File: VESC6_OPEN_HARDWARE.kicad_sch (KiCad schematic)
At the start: 21 parts, among them P1 USB_OTG, P2 TS_CAN, P3 SWD, P4 HALL/Encoder, P7 Custom

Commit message: started power stage
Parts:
- removed TP1, TP2: TestPoint, TestPoint:TestPoint_Pad_D1.5mm, symbol Connector:TestPoint
- P7: symbol Intra-Drive-Motor-Controller-V1-rescue:Connector_10-Pin-SJG_KiCad_Library -> Connector:Conn_01x08_Pin

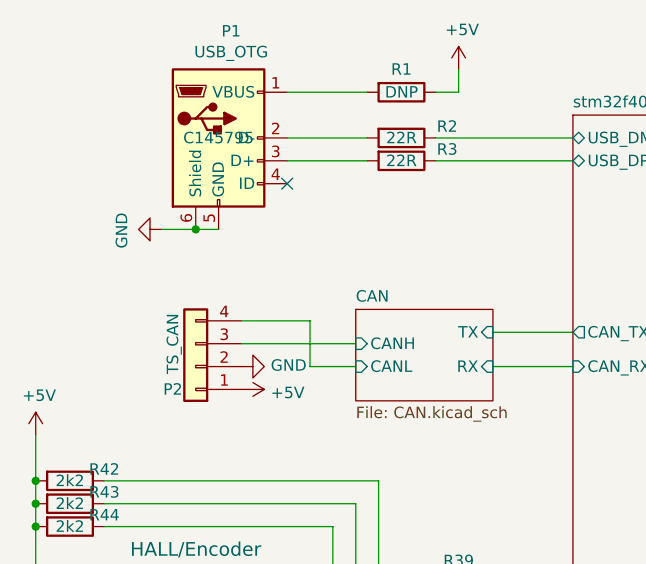
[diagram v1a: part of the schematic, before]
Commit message: more routing connectors and caps
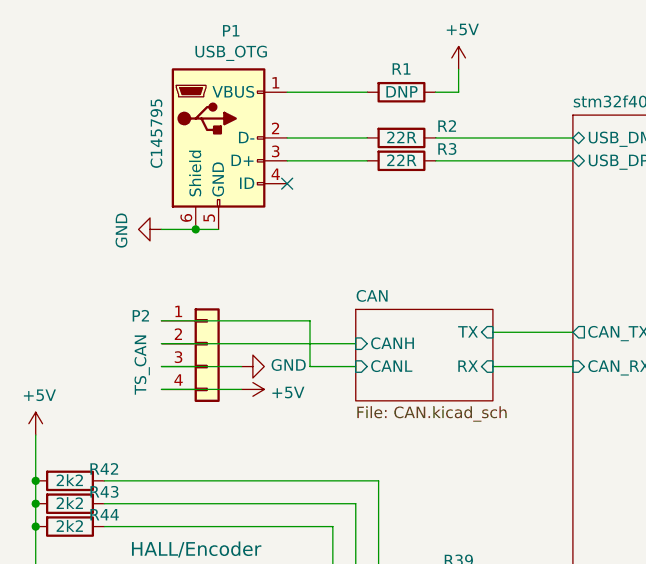
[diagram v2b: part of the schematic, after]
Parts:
- P2: footprint Connector_PinSocket_1.27mm:PinSocket_1x04_P1.27mm_Vertical -> Connector_JST:JST_SH_SM04B-SRSS-TB_1x04-1MP_P1.00mm_Horizontal
- P4: footprint Connector_PinSocket_1.27mm:PinSocket_1x06_P1.27mm_Vertical -> Connector_JST:JST_SH_SM06B-SRSS-TB_1x06-1MP_P1.00mm_Horizontal
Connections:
- net +5V: now also P2.4 (Pin_4); no longer P2.1 (Pin_1)
- net CAN/CANH: now also P2.2 (Pin_2); no longer P2.3 (Pin_3)
- net CAN/CANL: now also P2.1 (Pin_1); no longer P2.4 (Pin_4)
- net GND: now also P2.3 (Pin_3); no longer P2.2 (Pin_2)
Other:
- moved on the sheet: P2
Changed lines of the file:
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@@
 	(wire
 		(pts
-			(xy 91.44 49.53) (xy 99.06 49.53)
+			(xy 82.55 49.53) (xy 99.06 49.53)
 		)
 		(stroke
@@
 	(wire
 		(pts
+			(xy 82.55 57.15) (xy 91.44 57.15)
+		)
+		(stroke
+			(width 0)
+			(type default)
+		)
+	)
+	(wire
+		(pts
 			(xy 95.25 118.11) (xy 128.27 118.11)
 		)
@@
 	(wire
 		(pts
+			(xy 82.55 54.61) (xy 91.44 54.61)
+		)
+		(stroke
+			(width 0)
+			(type default)
+		)
+	)
+	(wire
+		(pts
 			(xy 121.92 128.27) (xy 128.27 128.27)
 		)
@@
 	(wire
 		(pts
-			(xy 91.44 52.07) (xy 104.14 52.07)
+			(xy 82.55 52.07) (xy 104.14 52.07)
 		)
 		(stroke
@@
 	(symbol
 		(lib_id "Connector_Generic:Conn_01x04")
-		(at 86.36 54.61 180)
+		(at 87.63 52.07 0)
 		(unit 1)
 		(exclude_from_sim no)
@@
 		(dnp no)
 		(property "Reference" "P2"
-			(at 83.82 57.15 0)
+			(at 80.264 49.022 0)
 			(effects
 				(font
@@
 		)
 		(property "Value" "TS_CAN"
-			(at 83.82 52.07 90)
+			(at 80.264 54.356 90)
 			(effects
 				(font
@@
 			)
 		)
-		(property "Footprint" "Connector_PinSocket_1.27mm:PinSocket_1x04_P1.27mm_Vertical"
-			(at 86.36 54.61 0)
+		(property "Footprint" "Connector_JST:JST_SH_SM04B-SRSS-TB_1x04-1MP_P1.00mm_Horizontal"
+			(at 87.63 52.07 0)
 			(effects
 				(font
@@
 		)
 		(property "Datasheet" "https://www.molex.com/content/dam/molex/molex-dot-com/products/automated/en-us/salesdrawingpdf/505/505567/5055670471_sd.pdf?inline"
-			(at 86.36 54.61 0)
+			(at 87.63 52.07 0)
 			(effects
 				(font
@@
 		)
 		(property "Description" ""
-			(at 86.36 54.61 0)
+			(at 87.63 52.07 0)
 			(effects
 				(font
@@
 		)
 		(property "LCSC part no." "C563985"
-			(at 86.36 54.61 0)
+			(at 87.63 52.07 0)
 			(effects
 				(font
@@
 		)
 		(property "Critical" "Y"
-			(at 86.36 54.61 0)
+			(at 87.63 52.07 0)
 			(effects
 				(font
@@
 		)
 		(property "Link" ""
-			(at 86.36 54.61 0)
+			(at 87.63 52.07 0)
 			(effects
 				(font
@@
 		)
 		(property "MFP" ""
-			(at 86.36 54.61 0)
+			(at 87.63 52.07 0)
 			(effects
 				(font
@@
 		)
 		(property "LCSC part no." "C145795"
-			(at 88.9 29.21 0)
+			(at 82.042 28.702 90)
 			(effects
 				(font
@@
 			)
 		)
-		(property "Footprint" "Connector_PinSocket_1.27mm:PinSocket_1x06_P1.27mm_Vertical"
+		(property "Footprint" "Connector_JST:JST_SH_SM06B-SRSS-TB_1x06-1MP_P1.00mm_Horizontal"
 			(at 86.36 83.82 0)
 			(effects

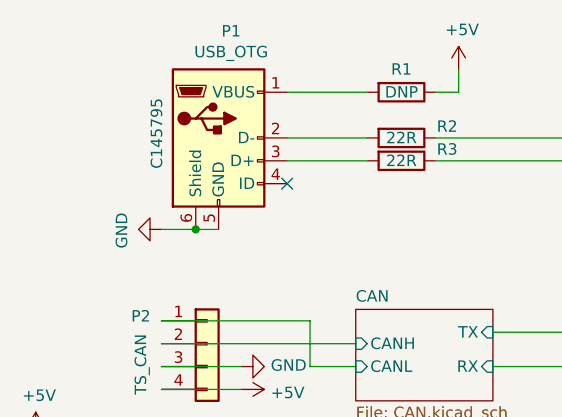
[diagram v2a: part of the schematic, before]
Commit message: More routing, positioning and SMT USB
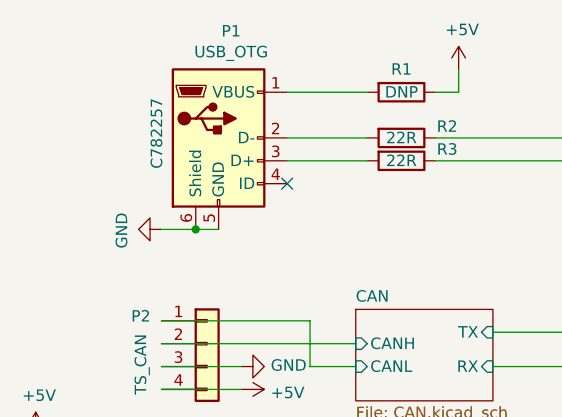
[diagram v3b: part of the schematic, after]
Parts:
- P1: footprint Connector_USB:USB_Micro-B_Wuerth_614105150721_Vertical -> Connector_USB:USB_Micro-B_Molex-105133-0001; LCSC part no. C145795 -> C782257
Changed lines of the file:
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@@
 			)
 		)
-		(property "Footprint" "Connector_USB:USB_Micro-B_Wuerth_614105150721_Vertical"
+		(property "Footprint" "Connector_USB:USB_Micro-B_Molex-105133-0001"
 			(at 92.71 30.48 0)
 			(effects
@@
 			)
 		)
-		(property "LCSC part no." "C145795"
+		(property "LCSC part no." "C782257"
 			(at 82.042 28.702 90)
 			(effects

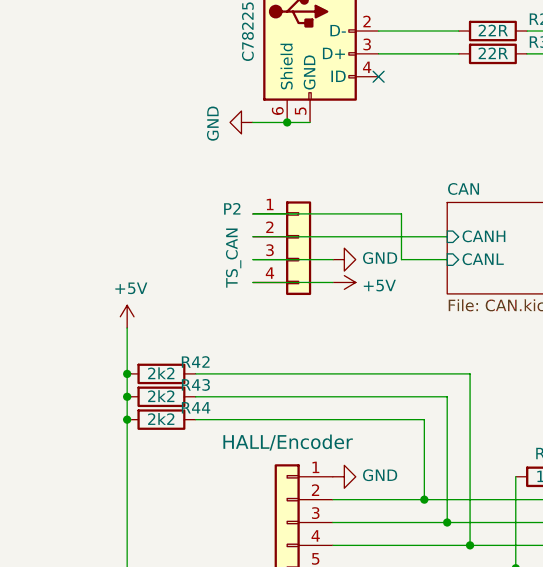
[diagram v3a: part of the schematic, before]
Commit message: double CAN ports
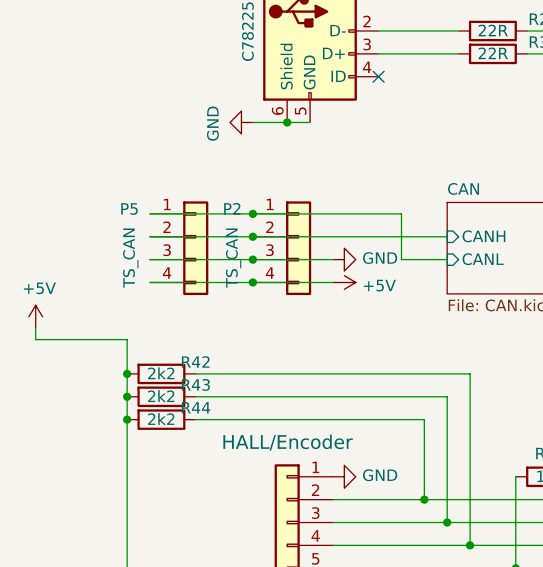
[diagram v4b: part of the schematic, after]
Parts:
- added P5: TS_CAN, Connector_JST:JST_SH_SM04B-SRSS-TB_1x04-1MP_P1.00mm_Horizontal, symbol Connector_Generic:Conn_01x04
- P2: LCSC part no. C563985 -> C160404
- P4: LCSC part no. C585388 -> C160405
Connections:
- net +5V: now also P5.4 (Pin_4)
- net CAN/CANH: now also P5.2 (Pin_2)
- net CAN/CANL: now also P5.1 (Pin_1)
- net GND: now also P5.3 (Pin_3)
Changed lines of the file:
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@@
 	)
 	(junction
+		(at 82.55 54.61)
+		(diameter 0)
+		(color 0 0 0 0)
+	)
+	(junction
 		(at 228.6 146.05)
 		(diameter 0)
@@
 	)
 	(junction
+		(at 82.55 52.07)
+		(diameter 0)
+		(color 0 0 0 0)
+	)
+	(junction
+		(at 82.55 49.53)
+		(diameter 0)
+		(color 0 0 0 0)
+	)
+	(junction
+		(at 82.55 57.15)
+		(diameter 0)
+		(color 0 0 0 0)
+	)
+	(junction
 		(at 228.6 142.24)
 		(diameter 0)
@@
 	(wire
 		(pts
+			(xy 58.42 63.5) (xy 68.58 63.5)
+		)
+		(stroke
+			(width 0)
+			(type default)
+		)
+	)
+	(wire
+		(pts
 			(xy 91.44 83.82) (xy 104.14 83.82)
 		)
@@
 	(wire
 		(pts
+			(xy 71.12 54.61) (xy 82.55 54.61)
+		)
+		(stroke
+			(width 0)
+			(type default)
+		)
+	)
+	(wire
+		(pts
 			(xy 203.2 138.43) (xy 208.28 138.43)
 		)
@@
 	(wire
 		(pts
+			(xy 68.58 63.5) (xy 68.58 67.31)
+		)
+		(stroke
+			(width 0)
+			(type default)
+		)
+	)
+	(wire
+		(pts
 			(xy 190.5 138.43) (xy 190.5 135.89)
 		)
@@
 	(wire
 		(pts
-			(xy 68.58 67.31) (xy 68.58 62.23)
+			(xy 58.42 63.5) (xy 58.42 62.23)
 		)
 		(stroke
@@
 	(wire
 		(pts
+			(xy 71.12 57.15) (xy 82.55 57.15)
+		)
+		(stroke
+			(width 0)
+			(type default)
+		)
+	)
+	(wire
+		(pts
 			(xy 104.14 69.85) (xy 104.14 83.82)
 		)
@@
 	(wire
 		(pts
+			(xy 71.12 49.53) (xy 82.55 49.53)
+		)
+		(stroke
+			(width 0)
+			(type default)
+		)
+	)
+	(wire
+		(pts
 			(xy 91.44 146.05) (xy 128.27 146.05)
 		)
@@
 	(wire
 		(pts
+			(xy 71.12 52.07) (xy 82.55 52.07)
+		)
+		(stroke
+			(width 0)
+			(type default)
+		)
+	)
+	(wire
+		(pts
 			(xy 91.44 148.59) (xy 128.27 148.59)
 		)
@@
 			)
 		)
-		(property "LCSC part no." "C563985"
+		(property "LCSC part no." "C160404"
 			(at 87.63 52.07 0)
 			(effects
@@
 	(symbol
 		(lib_id "power:+5V")
-		(at 68.58 62.23 0)
+		(at 58.42 62.23 0)
 		(unit 1)
 		(exclude_from_sim no)
@@
 		(dnp no)
 		(property "Reference" "#PWR04"
-			(at 68.58 66.04 0)
+			(at 58.42 66.04 0)
 			(effects
 				(font
@@
 		)
 		(property "Value" "+5V"
-			(at 68.961 57.8358 0)
+			(at 58.801 57.8358 0)
 			(effects
 				(font
@@
 		)
 		(property "Footprint" ""
-			(at 68.58 62.23 0)
+			(at 58.42 62.23 0)
 			(effects
 				(font
@@
 		)
 		(property "Datasheet" ""
-			(at 68.58 62.23 0)
+			(at 58.42 62.23 0)
 			(effects
 				(font
@@
 		)
 		(property "Description" ""
-			(at 68.58 62.23 0)
+			(at 58.42 62.23 0)
 			(effects
 				(font
@@
 	)
 	(symbol
+		(lib_id "Connector_Generic:Conn_01x04")
+		(at 76.2 52.07 0)
+		(unit 1)
+		(exclude_from_sim no)
+		(in_bom yes)
+		(on_board yes)
+		(dnp no)
+		(property "Reference" "P5"
+			(at 68.834 49.022 0)
+			(effects
+				(font
+					(size 1.27 1.27)
+				)
+			)
+		)
+		(property "Value" "TS_CAN"
+			(at 68.834 54.356 90)
+			(effects
+				(font
+					(size 1.27 1.27)
+				)
+			)
+		)
+		(property "Footprint" "Connector_JST:JST_SH_SM04B-SRSS-TB_1x04-1MP_P1.00mm_Horizontal"
+			(at 76.2 52.07 0)
+			(effects
+				(font
+					(size 1.27 1.27)
+				)
+				(hide yes)
+			)
+		)
+		(property "Datasheet" "https://www.molex.com/content/dam/molex/molex-dot-com/products/automated/en-us/salesdrawingpdf/505/505567/5055670471_sd.pdf?inline"
+			(at 76.2 52.07 0)
+			(effects
+				(font
+					(size 1.27 1.27)
+				)
+				(hide yes)
+			)
+		)
+		(property "Description" ""
+			(at 76.2 52.07 0)
+			(effects
+				(font
+					(size 1.27 1.27)
+				)
+				(hide yes)
+			)
+		)
+		(property "LCSC part no." "C160404"
+			(at 76.2 52.07 0)
+			(effects
+				(font
+					(size 1.27 1.27)
+				)
+				(hide yes)
+			)
+		)
+		(property "Critical" "Y"
+			(at 76.2 52.07 0)
+			(effects
+				(font
+					(size 1.27 1.27)
+				)
+				(hide yes)
+			)
+		)
+		(property "Link" ""
+			(at 76.2 52.07 0)
+			(effects
+				(font
+					(size 1.27 1.27)
+				)
+				(hide yes)
+			)
+		)
+		(property "MFP" ""
+			(at 76.2 52.07 0)
+			(effects
+				(font
+					(size 1.27 1.27)
+				)
+				(hide yes)
+			)
+		)
+		(pin "1"
+		)
+		(pin "2"
+		)
+		(pin "3"
+		)
+		(pin "4"
+		)
+		(instances
+			(project "VESC6_OPEN_HARDWARE"
+				(path "/8bc2c25a-a1f1-4ce8-b96a-a4f8f4c35079"
+					(reference "P5")
+					(unit 1)
+				)
+			)
+		)
+	)
+	(symbol
 		(lib_id "power:GND")
 		(at 91.44 54.61 90)
@@
 			)
 		)
-		(property "LCSC part no." "C585388"
+		(property "LCSC part no." "C160405"
 			(at 86.36 83.82 0)
 			(effects

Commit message: Adjusted connectors and routing
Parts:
- P3: footprint Connector_PinSocket_1.27mm:PinSocket_1x06_P1.27mm_Vertical -> Connector_JST:JST_SH_SM06B-SRSS-TB_1x06-1MP_P1.00mm_Horizontal
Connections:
- net +5V: now also P3.1 (Pin_1)
- net GND: now also P3.4 (Pin_4); no longer P3.3 (Pin_3)
- net VCC: now also P3.6 (Pin_6); no longer P3.1 (Pin_1)
- net stm32f40x/NRST: now also P3.2 (Pin_2); no longer P3.5 (Pin_5)
- net stm32f40x/SWCLK: now also P3.5 (Pin_5); no longer P3.2 (Pin_2)
- net stm32f40x/SWDIO: now also P3.3 (Pin_3); no longer P3.4 (Pin_4)
- no-connect marks 2 -> 1
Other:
- moved on the sheet: P3
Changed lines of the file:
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@@
 		(at 96.52 34.29)
 	)
-	(no_connect
-		(at 91.44 151.13)
-	)
 	(wire
 		(pts
@@
 	(wire
 		(pts
+			(xy 83.82 143.51) (xy 91.44 143.51)
+		)
+		(stroke
+			(width 0)
+			(type default)
+		)
+	)
+	(wire
+		(pts
 			(xy 99.06 49.53) (xy 99.06 54.61)
 		)
@@
 	(wire
 		(pts
+			(xy 83.82 138.43) (xy 91.44 138.43)
+		)
+		(stroke
+			(width 0)
+			(type default)
+		)
+	)
+	(wire
+		(pts
 			(xy 96.52 24.13) (xy 105.41 24.13)
 		)
@@
 	(wire
 		(pts
-			(xy 128.27 140.97) (xy 91.44 140.97)
+			(xy 128.27 140.97) (xy 83.82 140.97)
 		)
 		(stroke
@@
 	(wire
 		(pts
-			(xy 91.44 146.05) (xy 128.27 146.05)
+			(xy 83.82 146.05) (xy 128.27 146.05)
 		)
 		(stroke
@@
 	(wire
 		(pts
-			(xy 91.44 148.59) (xy 128.27 148.59)
+			(xy 83.82 148.59) (xy 128.27 148.59)
 		)
 		(stroke
@@
 		(dnp no)
 		(property "Reference" "R44"
-			(at 76.2 71.12 90)
+			(at 77.978 71.374 90)
 			(effects
 				(font
@@
 		(dnp no)
 		(property "Reference" "R43"
-			(at 76.2 68.58 90)
+			(at 77.978 68.58 90)
 			(effects
 				(font
@@
 		(dnp no)
 		(property "Reference" "R42"
-			(at 76.2 66.04 90)
+			(at 77.978 66.294 90)
 			(effects
 				(font
@@
 			)
 		)
-		(property "Datasheet" "https://datasheet.lcsc.com/lcsc/1811151141_Korean-Hroparts-Elec-U-D-M5DD-W-1_C145795.pdf"
+		(property "Datasheet" "https://www.molex.com/content/dam/molex/molex-dot-com/products/automated/en-us/salesdrawingpdf/482/48258/482580001_sd.pdf?"
 			(at 92.71 30.48 0)
 			(effects
@@
 	)
 	(symbol
+		(lib_id "power:+5V")
+		(at 83.82 151.13 270)
+		(unit 1)
+		(exclude_from_sim no)
+		(in_bom yes)
+		(on_board yes)
+		(dnp no)
+		(property "Reference" "#PWR0121"
+			(at 80.01 151.13 0)
+			(effects
+				(font
+					(size 1.27 1.27)
+				)
+				(hide yes)
+			)
+		)
+		(property "Value" "+5V"
+			(at 87.0712 151.511 90)
+			(effects
+				(font
+					(size 1.27 1.27)
+				)
+				(justify left)
+			)
+		)
+		(property "Footprint" ""
+			(at 83.82 151.13 0)
+			(effects
+				(font
+					(size 1.27 1.27)
+				)
+				(hide yes)
+			)
+		)
+		(property "Datasheet" ""
+			(at 83.82 151.13 0)
+			(effects
+				(font
+					(size 1.27 1.27)
+				)
+				(hide yes)
+			)
+		)
+		(property "Description" ""
+			(at 83.82 151.13 0)
+			(effects
+				(font
+					(size 1.27 1.27)
+				)
+			)
+		)
+		(pin "1"
+		)
+		(instances
+			(project "VESC6_OPEN_HARDWARE"
+				(path "/8bc2c25a-a1f1-4ce8-b96a-a4f8f4c35079"
+					(reference "#PWR0121")
+					(unit 1)
+				)
+			)
+		)
+	)
+	(symbol
 		(lib_id "power:GND")
 		(at 115.57 102.87 90)
@@
 	(symbol
 		(lib_id "Connector_Generic:Conn_01x06")
-		(at 86.36 143.51 0)
-		(mirror y)
+		(at 88.9 146.05 0)
+		(mirror x)
 		(unit 1)
 		(exclude_from_sim no)
@@
 		(dnp no)
 		(property "Reference" "P3"
-			(at 86.36 153.67 0)
+			(at 88.9 135.89 0)
 			(effects
 				(font
@@
 		)
 		(property "Value" "SWD"
-			(at 86.36 134.62 0)
+			(at 88.9 154.94 0)
 			(effects
 				(font
@@
 			)
 		)
-		(property "Footprint" "Connector_PinSocket_1.27mm:PinSocket_1x06_P1.27mm_Vertical"
-			(at 86.36 143.51 0)
+		(property "Footprint" "Connector_JST:JST_SH_SM06B-SRSS-TB_1x06-1MP_P1.00mm_Horizontal"
+			(at 88.9 146.05 0)
 			(effects
 				(font
@@
 		)
 		(property "Datasheet" "https://www.molex.com/content/dam/molex/molex-dot-com/products/automated/en-us/salesdrawingpdf/505/505567/5055670671_sd.pdf?inline"
-			(at 86.36 143.51 0)
+			(at 88.9 146.05 0)
 			(effects
 				(font
@@
 		)
 		(property "Description" ""
-			(at 86.36 143.51 0)
+			(at 88.9 146.05 0)
 			(effects
 				(font
@@
 		)
 		(property "LCSC part no." "C160405"
-			(at 86.36 143.51 0)
+			(at 88.9 146.05 0)
 			(effects
 				(font
@@
 		)
 		(property "Critical" "Y"
-			(at 86.36 143.51 0)
+			(at 88.9 146.05 0)
 			(effects
 				(font
@@
 		)
 		(property "Link" ""
-			(at 86.36 143.51 0)
+			(at 88.9 146.05 0)
 			(effects
 				(font
@@
 		)
 		(property "MFP" ""
-			(at 86.36 143.51 0)
+			(at 88.9 146.05 0)
 			(effects
 				(font

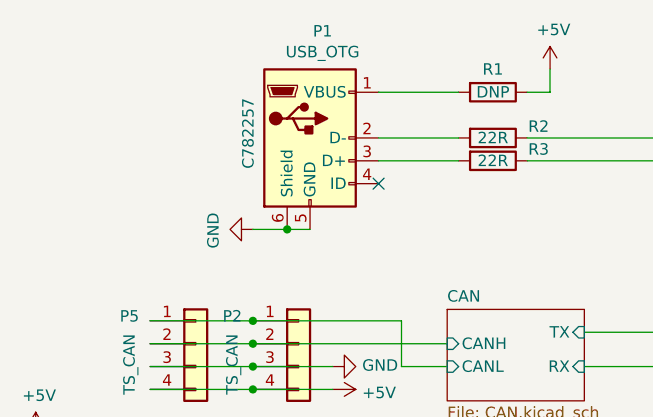
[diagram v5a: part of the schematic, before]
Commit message: Board resized and changed usb port
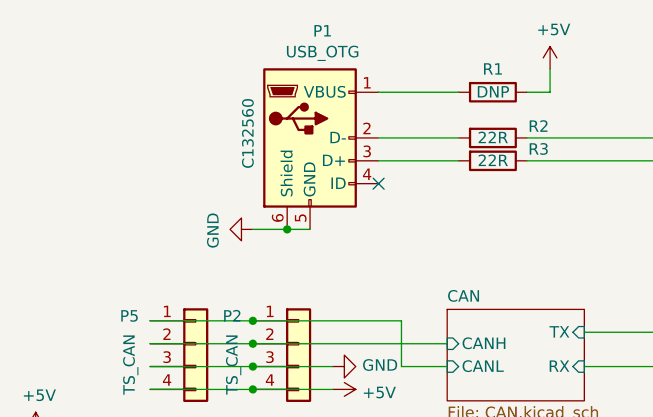
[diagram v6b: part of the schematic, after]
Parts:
- P1: footprint Connector_USB:USB_Micro-B_Molex-105133-0001 -> Connector_USB:USB_Micro-B_Molex_47346-0001; LCSC part no. C782257 -> C132560
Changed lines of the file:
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@@
 			)
 		)
-		(property "Footprint" "Connector_USB:USB_Micro-B_Molex-105133-0001"
+		(property "Footprint" "Connector_USB:USB_Micro-B_Molex_47346-0001"
 			(at 92.71 30.48 0)
 			(effects
@@
 			)
 		)
-		(property "LCSC part no." "C782257"
+		(property "LCSC part no." "C132560"
 			(at 82.042 28.702 90)
 			(effects
